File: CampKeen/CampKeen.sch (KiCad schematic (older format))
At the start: 172 parts, among them IC1 LM2597MX-5.0_NOPB, IC2 DS3231SN#, IC3 TL071CP, IC4 TL071CP, J1 Vin, J10 GenHeadL, J11 GenHeadR, J12 IO1, J2 5VJumper, J3 Temps, J4 CAC, J5 Tanks, J6 VAC, J7 IO1, J8 IO, J9 GenEnclosure, K1 DIP05-1A72-12L, K2 DIP05-1A72-12L, K3 DIP05-1A72-12L, K4 DIP05-1A72-12L, P1 Power, P10 CONN_01X01, P11 CONN_01X01, P12 CONN_01X01, P13 CONN_01X01, P2 Analog, P3 Analog, P4 Digital, P5 PWM, P6 PWM, P7 Communication, P8 CONN_01X01, P9 CONN_01X01, Q1 BC547, Q10 2N7000, Q11 2N7000, Q12 IRF510, Q13 2N7000, Q14 2N7000, Q15 BC547, Q16 IRF510, Q17 IRF510, Q18 IRF510, Q19 IRF510, Q2 2N7000, Q20 IRF510, Q21 2N7000, Q22 IRF510, Q23 2N7000, Q24 2N7000, Q25 BC547, Q26 IRF510, Q27 IRF510, Q28 2N7000, Q29 2N7000, Q3 2N7000, Q30 2N7000, Q31 2N7000, Q32 IRF510, Q33 2N7000, Q34 2N7000, Q35 IRF510, Q4 2N7000, Q5 2N7000, Q6 BC547, Q7 2N7000, Q8 2N7000, Q9 2N7000, T1 F24-045-C2, U1 TL431LP, U5 MAX232

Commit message: fixing values for resistors.
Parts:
- removed J12: IO1, SamacSys_Parts:1727751, symbol SamacSys_Parts:1727751
- added IC5: TL071CP, SamacSys_Parts:DIP794W53P254L959H508Q8N, symbol SamacSys_Parts:TL071CP
- added J3: Screw_Terminal_01x04, TerminalBlock_TE-Connectivity:TerminalBlock_TE_282834-4_1x04_P2.54mm_Horizontal, symbol Connector:Screw_Terminal_01x04
- added O1: O1, SamacSys_Parts:1727751, symbol SamacSys_Parts:1727751
- added Q36, Q37, Q38: 2N7000, Package_TO_SOT_THT:TO-92_Inline, symbol Transistor_FET:2N7000
- added Q39: IRF510, SamacSys_Parts:TO254P465X1024X2050-3P, symbol SamacSys_Parts:IRF510
- added R79, R80, R81, R82, R83, R84, R85: 1M, Resistor_THT:R_Axial_DIN0207_L6.3mm_D2.5mm_P7.62mm_Horizontal, symbol Device:R
- C6: value 1000uF -> 100nF
- I1: renamed from J8; value IO -> I1
- IO2: renamed from J7; value IO1 -> IO2
- R10, R12, R14, R15, R16, R21, R22, R23, R24, R25, R26, R27, R28, R29, R30, R32, R33, R34, R35, R46, R47, R50, R51, R52, R53, R56, R57, R58, R59, R60, R61, R62, R64, R65, R66, R67, R69, R8: value 100k -> 1M
- R19, R36, R4, R54: value R -> 10k
- R20, R37, R5, R55: value R -> 100k
- R31, R38, R39, R40, R42, R44, R45, R48, R49, R63, R68: value 47k -> 1M
- R6, R7: value 100K -> 1M
- T1: footprint F24045C2 -> SamacSys_Parts:F24045C2
- renumbered J5 to Tanks2, J3 to Temps1
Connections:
- net +12V: no longer Tanks1.2
- net +5V: now also IC5.7 (VCC+), J3.4 (Pin_4), Q36.3 (D), Q37.3 (D), Q38.3 (D)
- net 10(**): now also Q34.1 (S), R69.1; no longer Q28.1 (S), R57.1
- net 11(**): now also Q33.1 (S), R66.1; no longer Q27.1, R49.1
- net 12(**): now also Q31.1 (S), R64.1; no longer Q26.1, R48.1
- net 13(**): no longer Q22.1, R45.1
- net 14(Tx3): now also U5.10 (T2IN)
- net 15(Rx3): now also U5.9 (R2OUT)
- net 18(Tx1): now also Q36.1 (S), R80.1; no longer U5.10 (T2IN)
- net 19(Rx1): now also Q37.1 (S), R82.1; no longer U5.9 (R2OUT)
- net 2(**): now also Q13.1 (S), R33.1
- net 20(SDA): now also J3.1 (Pin_1); no longer IO2.12
- net 21(SCL): now also J3.2 (Pin_2); no longer IO2.11
- net 24: now also Q28.1 (S), R57.1; no longer Q35.1, R68.1
- net 25: now also Q23.1 (S), R51.1; no longer Q13.1 (S), R33.1
- net 27: now also Q30.1 (S), R61.1; no longer Q14.1 (S), R35.1
- net 3(**): now also Q14.1 (S), R35.1
- net 41: now also Q29.1 (S), R59.1; no longer Q20.1, R44.1
- net 5(**): now also Q27.1, R49.1; no longer Q34.1 (S), R69.1
- net 6(**): now also Q26.1, R48.1; no longer Q33.1 (S), R66.1
- net 7(**): now also Q22.1, R45.1; no longer Q31.1 (S), R64.1
- net 8(**): now also Q39.1, R85.1; no longer Q30.1 (S), R61.1
- net 9(**): now also Q35.1, R68.1; no longer Q29.1 (S), R59.1
- net A1: now also IO2.6; no longer IO2.8
- net A12: now also C6.1, J4.2 (Pin_2), R13.1, IC5.2 (IN-), IC5.6 (OUT); no longer J4.1 (Pin_1), R13.2
- net A13: now also IO2.11; no longer IO2.10
- net A14: now also Tanks2.11
- net A15: now also Tanks2.12
- net A2: now also IO2.12; no longer IO2.9
- net GND: now also IC5.4 (VCC-), J3.3 (Pin_3), Q39.3, R79.2, R80.2, R81.2, R82.2, R83.2, R84.2, R85.2; no longer IO2.3, IO2.6
- net at Q16.2: now also O1.1; no longer I1.3
- net +BATT: now reaches J1.1 (Pin_1), Main1.1
- net +BATT: now also Tanks1.2
- net at R78.1, U1.1 (REF), U1.3 (K): now also IC5.3 (IN+); no longer C6.1, J4.2 (Pin_2), R13.1
- net at Q11.2 (G), R29.1: now also I1.1; no longer Tanks2.11
- net at Q12.2: now also O1.12; no longer Tanks2.12
- net at Q32.2: now also O1.5; no longer I1.12
- net at U5.7 (T2OUT): now also IO2.3; no longer IO2.4
- net at U5.8 (R2IN): now also IO2.4; no longer IO2.5
- net at Q18.2: now also O1.3; no longer I1.5
- net at Q19.2: now also O1.4; no longer I1.6
- net at Q13.2 (G), R32.1: now also I1.2; no longer I1.1
- net at Q14.2 (G), R34.1: now also I1.3; no longer I1.2
- net at Q17.2: now also O1.2; no longer I1.4
- net at Q35.2: now also O1.6; no longer I1.10
- net at Q22.2: now also O1.9
- net at Q31.2 (G), R62.1: now also I1.9
- net at Q30.2 (G), R60.1: now also I1.10
- net at Q29.2 (G), R58.1: now also IO2.10
- net at Q20.2: now also O1.10
- net at Q26.2: now also O1.8
- net at Q27.2: now also O1.7
- net at Q28.2 (G), R56.1: now also IO2.9
- net at Q34.2 (G), R67.1: now also I1.7
- net at Q33.2 (G), R65.1: now also I1.8
- net at K3.1 (COM_1), K3.14 (COM_2): now also IO2.5; no longer IO2.7
- net at Q25.3 (E): now also O1.11; no longer I1.7
- net at Q24.2 (G), R52.1: now also I1.5; no longer I1.8
- net at Q23.2 (G), R50.1: now also I1.4; no longer I1.9
- removed net AlarmReset: P4.33 (Pin_33), Q23.1 (S), R51.1
- new net: Q20.1, R44.1
- new net: I1.12, Q37.2 (G), R81.1
- new net: I1.6, Q36.2 (G), R79.1
- new net: IO2.7, Q39.2
- new net: IO2.8, Q38.2 (G), R83.1
- new net: J4.1 (Pin_1), R13.2
- new net D22: P4.33 (Pin_33), Q38.1 (S), R84.1
- no-connect marks 40 -> 41
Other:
- moved on the sheet: C5, C6, I1, IC2, IO2, J2, J4, K1, K2, Q1, Q10, Q11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

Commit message: before freerouter
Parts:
- removed D1: 1N5817, SamacSys_Parts:DIOAD1414W86L464D238, symbol SamacSys_Parts:1N5817
- removed IC1: LM2597MX-5.0_NOPB, SamacSys_Parts:SOIC127P600X175-8N, symbol SamacSys_Parts:LM2597MX-5.0_NOPB
- removed J2: 5VJumper, Connector_PinHeader_2.54mm:PinHeader_1x02_P2.54mm_Vertical, symbol Connector_Generic:Conn_01x02
- added C1, C4: 0.1uF, Capacitor_THT:C_Rect_L9.0mm_W3.6mm_P7.50mm_MKT, symbol Device:C
- added C18: 15uF, Capacitor_THT:CP_Radial_D5.0mm_P2.50mm, symbol Device:CP
- added C2: 3.3nF, Capacitor_THT:C_Rect_L9.0mm_W3.6mm_P7.50mm_MKT, symbol Device:C
- added C6: 68uF, Capacitor_THT:CP_Radial_D5.0mm_P2.50mm, symbol Device:CP
- added C7: 120uF, Capacitor_THT:CP_Radial_D8.0mm_P5.00mm, symbol Device:CP
- added D2: 1N5817, SamacSys_Parts:DIOAD1414W86L464D238, symbol SamacSys_Parts:1N5817
- added IC1: LM2597MX-ADJ_NOPB, SamacSys_Parts:SOIC127P600X175-8N, symbol SamacSys_Parts:LM2597MX-ADJ_NOPB
- added IC2: LM2670SX-5.0_NOPB, SamacSys_Parts:LM2670SX50NOPB, symbol SamacSys_Parts:LM2670SX-5.0_NOPB
- added L1: 150mH, Inductor_THT:L_Axial_L9.5mm_D4.0mm_P15.24mm_Horizontal_Fastron_SMCC, symbol Device:L
- added Q40: IRF9Z34NPBF, SamacSys_Parts:TO254P469X1042X1967-3P, symbol SamacSys_Parts:IRF9Z34NPBF
- added R1: 4.7k, Resistor_THT:R_Axial_DIN0207_L6.3mm_D2.5mm_P7.62mm_Horizontal, symbol Device:R
- added R2: 1k, Resistor_THT:R_Axial_DIN0207_L6.3mm_D2.5mm_P7.62mm_Horizontal, symbol Device:R
- added R3: 6.2k, Resistor_THT:R_Axial_DIN0207_L6.3mm_D2.5mm_P7.62mm_Horizontal, symbol Device:R
- added R89: 100k, Resistor_THT:R_Axial_DIN0207_L6.3mm_D2.5mm_P7.62mm_Horizontal, symbol Device:R
- C3: renamed from C1; value 0.1uF -> 0.47uF
- C8: renamed from C2; value 0.1uF -> 0.01uF
- C9: renamed from C3; value 68uF -> 15uF
- L2: renamed from L1; value 100mH -> 33uH
- R4: renamed from R1; value 10k -> 1k
- renumbered C4 to C10, C6 to C11, C7 to C12, C8 to C13, C9 to C14, C10 to C15, C11 to C16, C12 to C17, D2 to D3, IC2 to IC3, IC3 to IC4, IC4 to IC5, IC5 to IC6, IO2 to IO1, J4 to J2, J6 to J3, J3 to J4, J9 to J5, J10 to J6, J11 to J7, K4 to K3, K3 to K4, Q13 to Q12, Q14 to Q13, Q23 to Q14, Q16 to Q15, Q24 to Q16, Q36 to Q18, Q18 to Q19, Q37 to Q20, Q19 to Q21, Q15 to Q22, Q21 to Q23, Q32 to Q24, Q30 to Q25, Q31 to Q26, Q35 to Q27, Q33 to Q28, Q12 to Q29, Q34 to Q30, Q39 to Q31, Q25 to Q32, Q28 to Q33, Q20 to Q34, Q29 to Q35, Q22 to Q36, Q38 to Q37, Q26 to Q38, Q27 to Q39, R7 to R10, R8 to R11, R10 to R12, R12 to R13, R70 to R16, R71 to R17, R16 to R18, R72 to R19, R73 to R20, R74 to R21, R75 to R22, R76 to R23, R77 to R24, R13 to R25, R19 to R26, R20 to R27, R9 to R28, R78 to R29, R11 to R30, R21 to R31, R22 to R32, R23 to R33, R24 to R34, R17 to R35, R18 to R36, R25 to R37, R26 to R38, R27 to R39, R28 to R40, R29 to R41, R30 to R42, R32 to R43, R33 to R44, R34 to R45, R35 to R46, R50 to R47, R51 to R48, R38 to R49, R2 to R5, R52 to R50, R53 to R51, R39 to R52, R79 to R53, R80 to R54, R81 to R55, R40 to R56, R82 to R57, R36 to R58, R46 to R59, R3 to R6, R42 to R60, R37 to R61, R47 to R62, R60 to R63, R63 to R64, R61 to R65, R62 to R66, R68 to R67, R64 to R68, R65 to R69, R4 to R7, R41 to R70, R31 to R71, R66 to R72, R67 to R73, R43 to R74, R69 to R75, R54 to R76, R85 to R77, R55 to R78, R56 to R79, R5 to R8, R57 to R80, R58 to R81, R44 to R82, R59 to R83, R45 to R84, R83 to R85, R84 to R86, R48 to R87, R49 to R88, R6 to R9, RV9 to RV1, RV10 to RV2, U5 to U2
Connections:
- net +12V: now also C3.1, C18.1, C6.1, IC1.7 (+VIN), IC2.2 (INPUT), Q40.3; no longer R4.1
- net +5P: no longer J5.1 (Pin_1), J6.1 (Pin_1), J7.1 (Pin_1)
- net +5V: now also J5.1 (Pin_1), J6.1 (Pin_1), J7.1 (Pin_1), IC2.6 (FEEDBACK/FB)
- net GND: now also R4.1, C1.2, C18.2, C4.2, C6.2, C7.2, D2.2, IC1.6 (GROUND), IC2.4 (GND), IC2.8 (EP), R2.2, R89.2; no longer C8.2
- net at Main1.2: now also Q40.2
- net at R4.2: now also IC2.5 (SYNC)
- net at C8.1: now also IC2.3 (CBOOST/CB)
- net at D3.1, L2.1: now also C8.2, IC2.1 (SWITCH_OUTPUT)
- net Vin renamed +9V
- net +9V: now also C2.2, C7.1, IC1.3 (BIAS_SUPPLY), L1.2, R1.2, R3.1
- new net: IC1.1 (ERROR_FLAG), R1.1
- new net: C1.1, IC1.2 (DELAY)
- new net: C2.1, IC1.4 (FEEDBACK), R2.1, R3.2
- new net: C4.1, IC1.5 (~SHUTDOWN~/SOFT-START)
- new net: D2.1, IC1.8 (OUTPUT), L1.1
- new net: Q40.1, R89.1
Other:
- moved on the sheet: C10, C11, C3, C8, C9, D3, IC6, J1, J2, L2, Main1, R25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

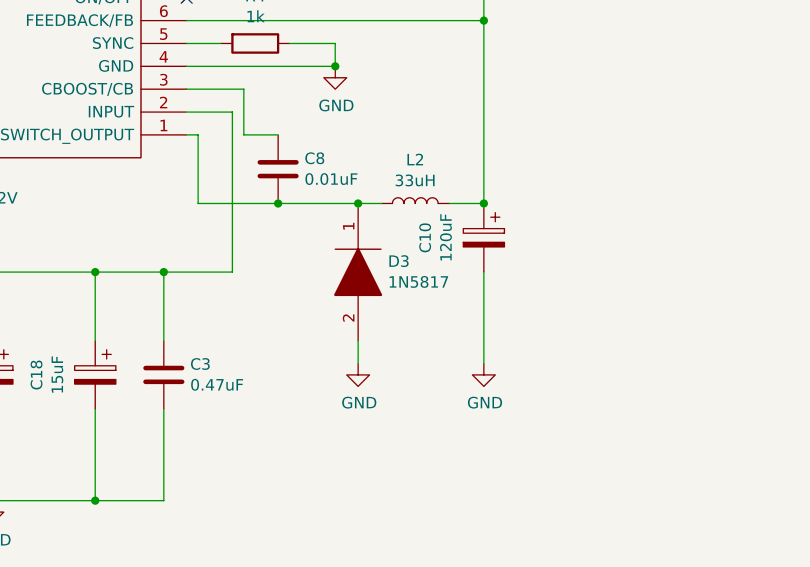
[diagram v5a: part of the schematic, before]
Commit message: fixed footprint for diode and pad for reg
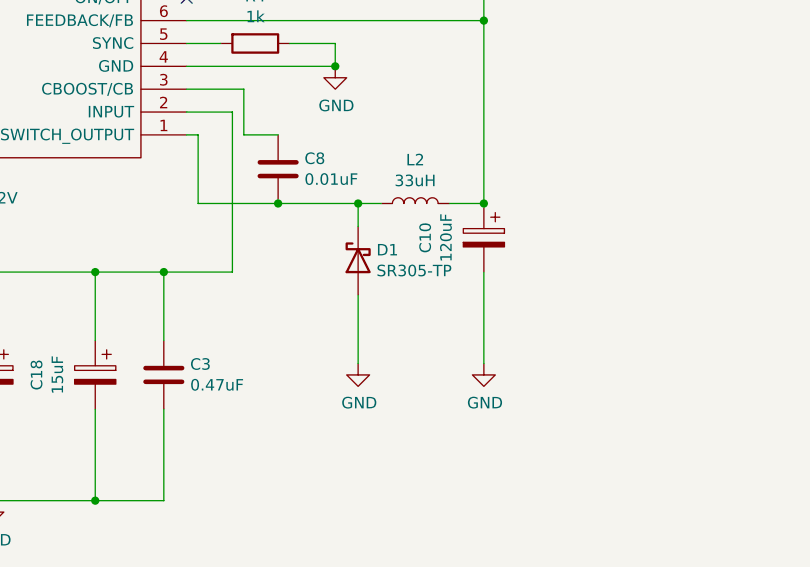
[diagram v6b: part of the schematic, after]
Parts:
- removed D3: 1N5817, SamacSys_Parts:DIOAD1414W86L464D238, symbol SamacSys_Parts:1N5817
- added D1: SR305-TP, Diode_THT:D_DO-201AD_P5.08mm_Vertical_AnodeUp, symbol Device:D_Schottky
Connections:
- net GND: now also D1.2 (A)
- net at C8.2, IC2.1 (SWITCH_OUTPUT), L2.1: now also D1.1 (K)
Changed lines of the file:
@@
 AlarmReset
 $Comp
-L SamacSys_Parts:1N5817 D3
-U 1 1 64E613FB
-P 6700 16400
-F 0 "D3" V 6954 16530 50  0000 L CNN
-F 1 "1N5817" V 7045 16530 50  0000 L CNN
-F 2 "SamacSys_Parts:DIOAD1414W86L464D238" H 7150 16400 50  0001 L CNN
-F 3 "http://www.st.com/web/en/resource/technical/document/datasheet/CD00001625.pdf" H 7150 16300 50  0001 L CNN
-F 4 "1N5817, Schottky Diode,  1A max, 20V, 2-Pin, DO-41" H 7150 16200 50  0001 L CNN "Description"
-F 5 "" H 7150 16100 50  0001 L CNN "Height"
-F 6 "511-1N5817" H 7150 16000 50  0001 L CNN "Mouser Part Number"
-F 7 "https://www.mouser.co.uk/ProductDetail/STMicroelectronics/1N5817?qs=JV7lzlMm3yKNnxZdh%252BSMnw%3D%3D" H 7150 15900 50  0001 L CNN "Mouser Price/Stock"
-F 8 "STMicroelectronics" H 7150 15800 50  0001 L CNN "Manufacturer_Name"
-F 9 "1N5817" H 7150 15700 50  0001 L CNN "Manufacturer_Part_Number"
-	1    6700 16400
-	0    1    1    0
-$EndComp
-$Comp
 L Device:C C3
 U 1 1 64EA7242
@@
 $EndComp
 Wire Wire Line
-	6700 17100 6700 17000
-Wire Wire Line
 	7250 17100 7250 16700
 $Comp
@@
 $EndComp
 Wire Wire Line
-	6800 16400 6700 16400
-Wire Wire Line
 	7100 16400 7250 16400
 $Comp
@@
 	6200 16100 6350 16100
 Wire Wire Line
-	6350 16400 6700 16400
-Connection ~ 6700 16400
-Wire Wire Line
 	7250 15200 7250 15600
 Connection ~ 7250 16400
@@
 	18150 25700 18150 26500
 Connection ~ 18150 25700
+$Comp
+L Device:D_Schottky D1
+U 1 1 61306BCB
+P 6700 16650
+F 0 "D1" V 6654 16570 50  0000 R CNN
+F 1 "SR305-TP" V 6745 16570 50  0000 R CNN
+F 2 "Diode_THT:D_DO-201AD_P5.08mm_Vertical_AnodeUp" H 6700 16650 50  0001 C CNN
+F 3 "~" H 6700 16650 50  0001 C CNN
+	1    6700 16650
+	0    -1   1    0
+$EndComp
+Wire Wire Line
+	6350 16400 6700 16400
+Wire Wire Line
+	6700 16500 6700 16400
+Connection ~ 6700 16400
+Wire Wire Line
+	6700 16400 6800 16400
+Wire Wire Line
+	6700 16800 6700 17100
 Wire Bus Line
 	8600 7000 25650 7000

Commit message: 0.2 version for fab
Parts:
- removed IC5, IC6: TL071CP, SamacSys_Parts:DIP794W53P254L959H508Q8N, symbol SamacSys_Parts:TL071CP
- removed RV2: 1M, Potentiometer_THT:Potentiometer_Bourns_3296W_Vertical, symbol Device:R_POT_US
- removed U1: TL431LP, Package_TO_SOT_THT:TO-92_Inline, symbol Reference_Voltage:TL431LP
- added R90: 100k, Resistor_THT:R_Axial_DIN0207_L6.3mm_D2.5mm_P7.62mm_Horizontal, symbol Device:R
- C11: value 100nF -> 10uF
- R29: value R -> 100k
- R36: value 47K -> 180k
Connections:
- net +5P: no longer U2.16 (VCC)
- net +5V: now also U2.16 (VCC)
- net A11: now also R30.1
- net A12: now also R29.1, R90.2
- net GND: now also R90.1
- no-connect marks 41 -> 36
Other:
- moved on the sheet: BR1, C11, C12, C13, J2, J3, K3, R25, R29, R30, T1, VACFuse1

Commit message: 0.3 wip plans for making more use of space and possibly moving some stuff around
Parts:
- removed Q34: IRF510, SamacSys_Parts:TO254P465X1024X2050-3P, symbol SamacSys_Parts:IRF510
- removed R82: 1M, Resistor_THT:R_Axial_DIN0207_L6.3mm_D2.5mm_P7.62mm_Horizontal, symbol Device:R
- R1, R10, R11, R12, R13, R14, R15, R16, R17, R18, R19, R2, R20, R21, R22, R23, R24, R25, R26, R27, R28, R29, R3, R30, R31, R32, R33, R34, R35, R36, R37, R38, R39, R4, R40, R41, R42, R43, R44, R45, R46, R47, R48, R49, R5, R50, R51, R52, R53, R54, R55, R56, R57, R58, R59, R6, R60, R61, R62, R63, R64, R65, R66, R67, R68, R69, R7, R70, R71, R72, R73, R74, R75, R76, R77, R78, R79, R8, R80, R81, R83, R84, R85, R86, R87, R88, R89, R9, R90: footprint Resistor_THT:R_Axial_DIN0207_L6.3mm_D2.5mm_P7.62mm_Horizontal -> Resistor_THT:R_Axial_DIN0207_L6.3mm_D2.5mm_P2.54mm_Vertical
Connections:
- net +9V: now also IO1.7
- net at O1.10: now also Q31.2
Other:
- moved on the sheet: Q31, R77
